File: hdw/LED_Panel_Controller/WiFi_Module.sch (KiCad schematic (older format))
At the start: 31 parts

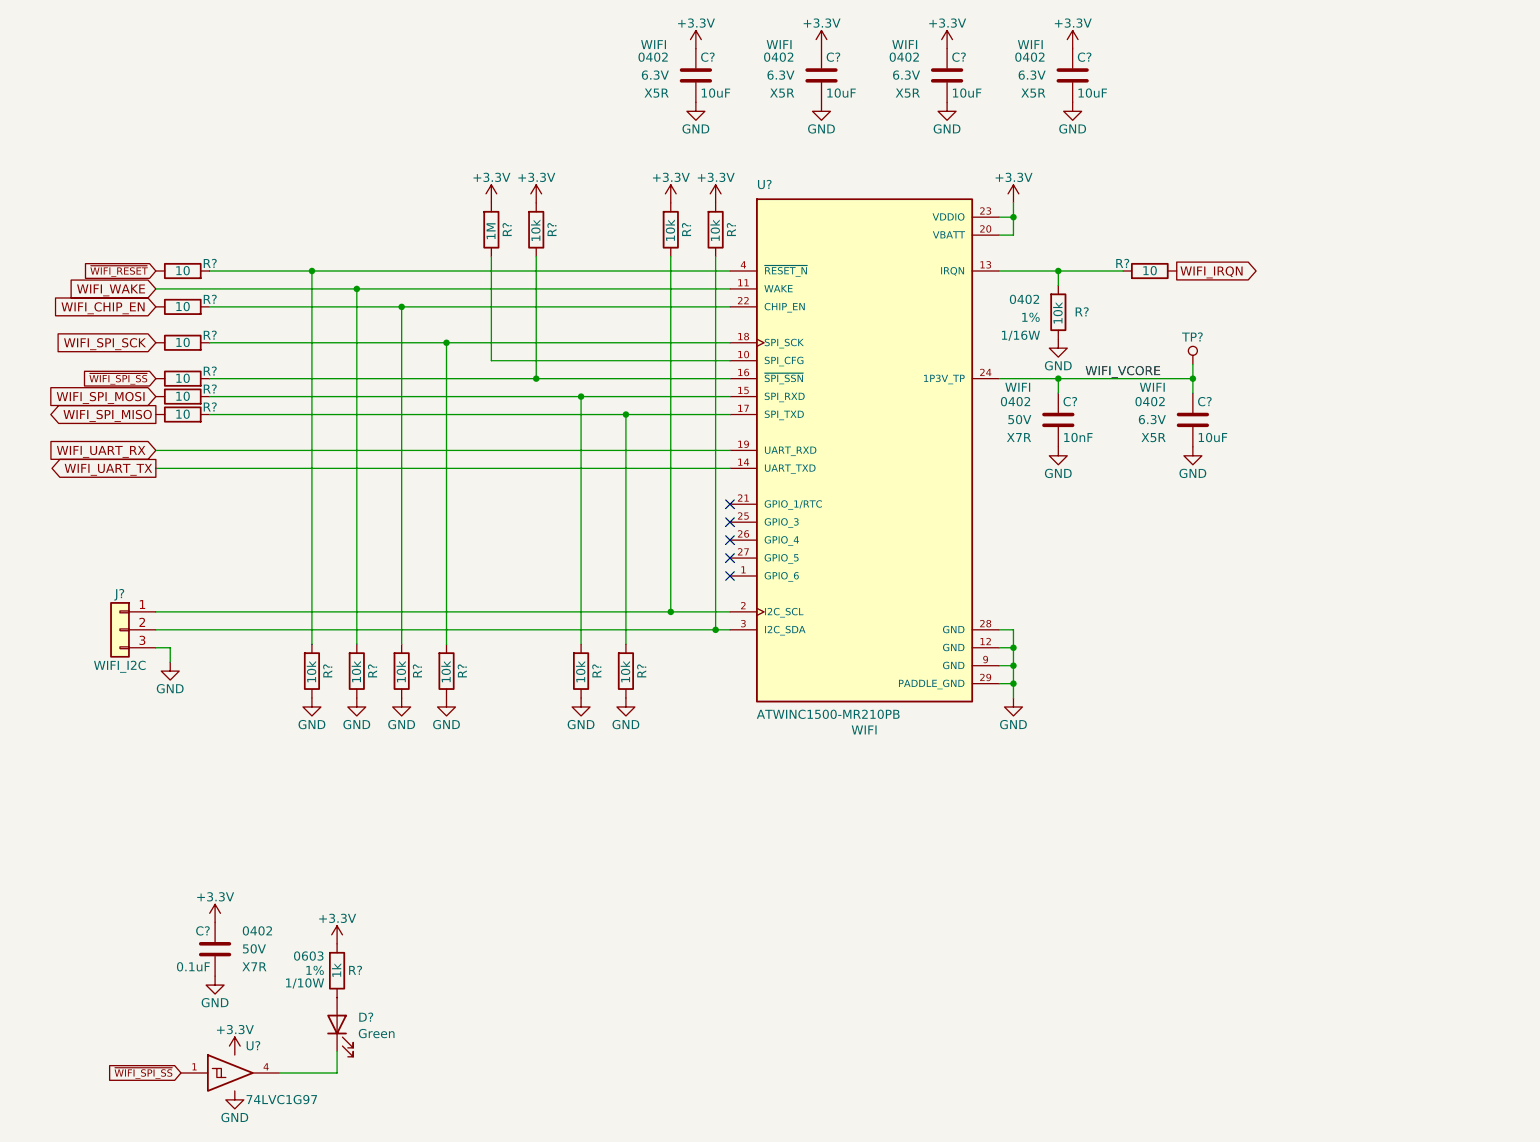
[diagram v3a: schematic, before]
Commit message: assigned a lot of nets to MCU pins
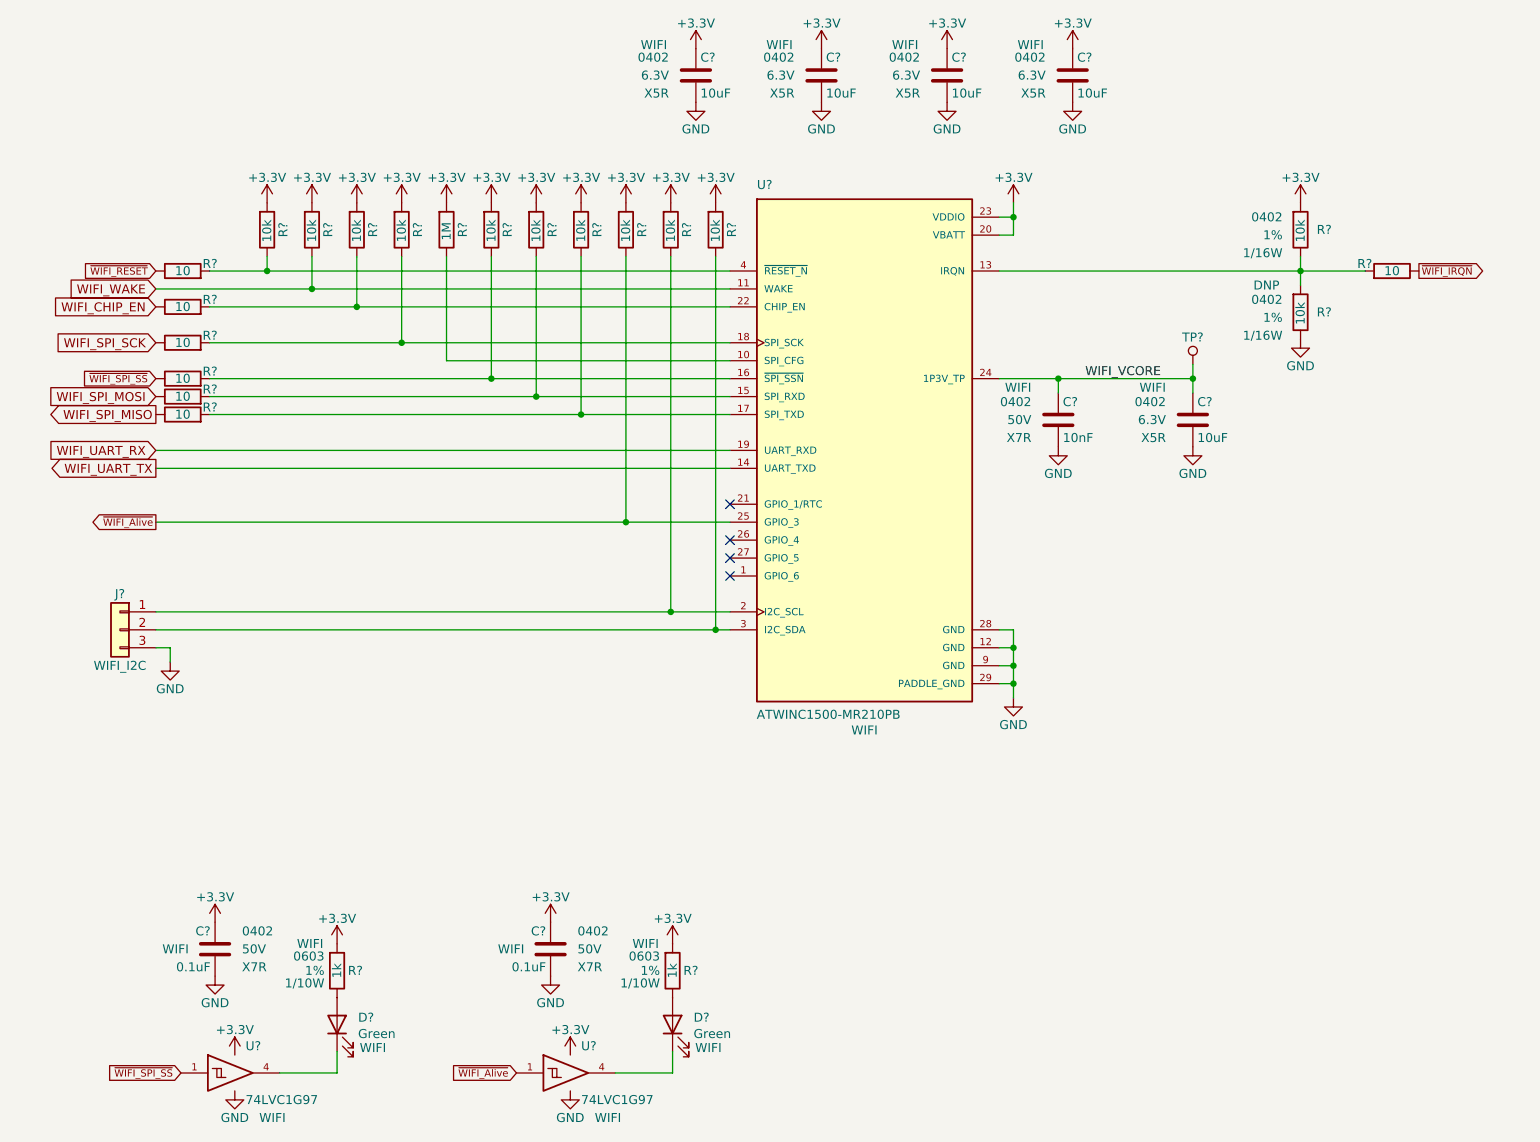
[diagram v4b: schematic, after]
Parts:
- added C?: 0.1uF, Capacitors_SMD:C_0402, symbol Custom_Library:C_Custom
- added D?: Green, LEDs:LED_0603, symbol Device:LED
- added R? (x2): 10k, Resistors_SMD:R_0402, symbol Custom_Library:R_Custom
- added R?: 1k, Resistors_SMD:R_0603, symbol Custom_Library:R_Custom
- added U?: 74LVC1G97, Package_TO_SOT_SMD:SOT-363_SC-70-6, symbol Custom_Library:74LVC1G97_Power_BUF
- C?, D?, R?, U?: Configuration (none) -> WIFI
- R?: Configuration (none) -> DNP
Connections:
- net +3V3: now also R?.1, R?.1, R?.1, R?.1, R?.1, R?.1, C?.1, R?.1, R?.1, R?.1, U?.5 (VCC)
- net GND: now also C?.2, U?.2 (GND), U?.3 (GND), U?.6 (GND); no longer R?.2, R?.2, R?.2, R?.2, R?.2, R?.2
- net WIFI_WAKE: now also R?.2; no longer R?.1
- net at R?.1, R?.1, U?.13 (IRQN): now also R?.2
- net at R?.1, U?.15 (SPI_RXD): now also R?.2; no longer R?.1
- net at R?.1, U?.16 (~SPI_SSN~): now also R?.2; no longer R?.2
- net at R?.1, U?.17 (SPI_TXD): now also R?.2; no longer R?.1
- net at R?.1, U?.18 (SPI_SCK): now also R?.2; no longer R?.1
- net at R?.1, U?.22 (CHIP_EN): now also R?.2; no longer R?.1
- net ~WIFI_Alive: now reaches U?.25 (GPIO_3)
- net ~WIFI_Alive: now also R?.2, U?.1
- net at R?.1, U?.4 (~RESET_N~): now also R?.2; no longer R?.1
- net WIFI_IRQN renamed ~WIFI_IRQN
- new net: D?.1 (K), U?.4
- new net: D?.2 (A), R?.2
- no-connect marks 5 -> 4
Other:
- moved on the sheet: R?
